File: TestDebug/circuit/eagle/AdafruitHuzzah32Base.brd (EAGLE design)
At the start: 64.4 x 47 mm, 5 parts, among them J1 CORTEX_DEBUG_PTH

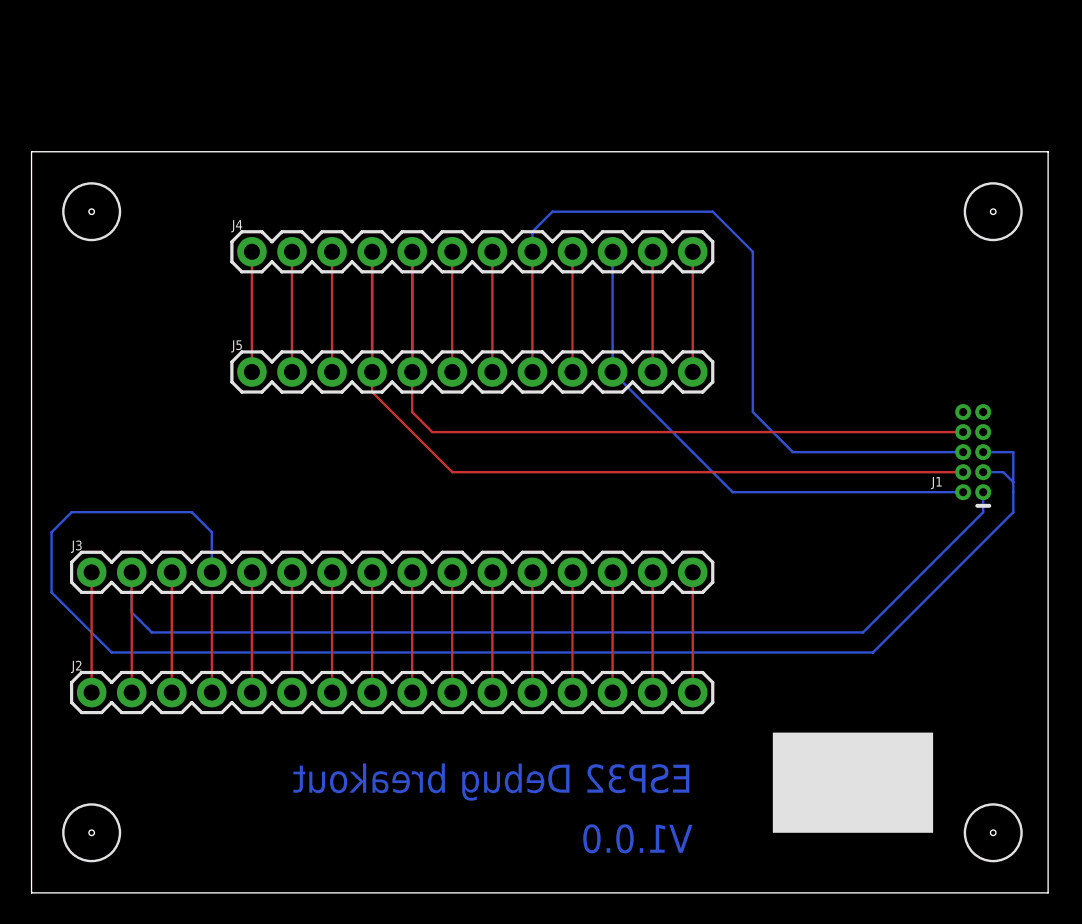
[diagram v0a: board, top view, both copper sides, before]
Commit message: Added power pins and more silk screen
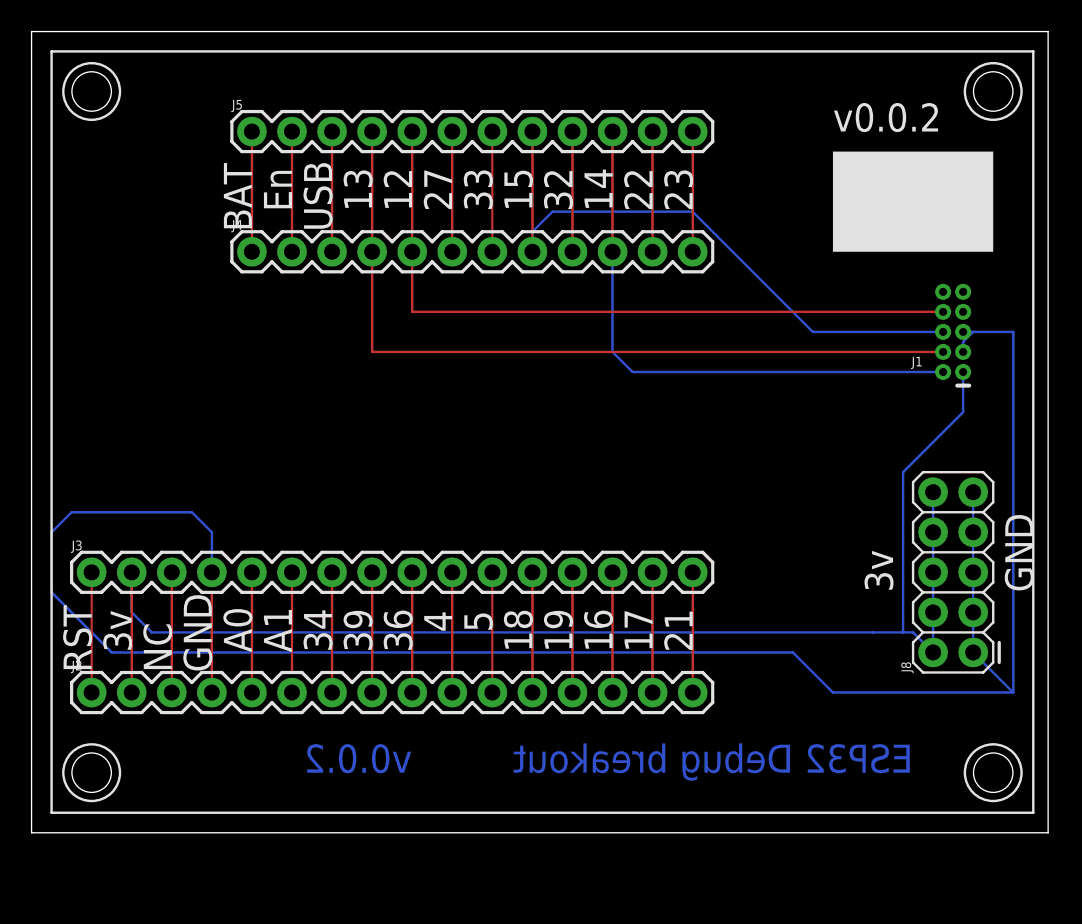
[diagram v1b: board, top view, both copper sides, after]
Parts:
- added J8: (no value), SparkFun-Connectors:2X5
- moved J5 15.2 mm to (17.8, 77.5)
- moved J1 7.73 mm to (62.2, 64.8)
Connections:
- net N$1: now also J8.10, J8.2, J8.4, J8.6, J8.8
- net N$2: now also J8.1, J8.3, J8.5, J8.7, J8.9
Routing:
- net N$2: track 98.0 -> 128.8 mm
- net N$1: track 69.1 -> 90.9 mm
- net N$3: track 49.0 -> 38.6 mm
- net N$4: track 53.2 -> 45.1 mm
- net N$5: track 56.1 -> 50.2 mm
- net N$6: track 33.0 -> 35.5 mm
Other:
- board size 64.4 x 47 mm -> 64.4 x 50.8 mm
- board text added: "12"
- board text added: "13"
- board text added: "14"
- board text added: "15"
- board text added: "16"
- board text added: "17"
- board text added: "18"
- board text added: "19"
- board text added: "21"
- board text added: "22"
- board text added: "23"
- board text added: "27"
- board text added: "32"
- board text added: "33"
- board text added: "34"
- board text added: "36"
- board text added: "39"
- board text added: "3v"
- board text added: "4"
- board text added: "5"
- board text added: "A0"
- board text added: "A1"
- board text added: "BAT"
- board text added: "En"
- board text added: "GND"
- board text added: "NC"
- board text added: "RST"
- board text added: "USB"
- board text added: "https://github.com/jastill/Platform-IO-Esp-Prog"
- board text added: "v0.0.2"
- board text removed: "V1.0.0"
